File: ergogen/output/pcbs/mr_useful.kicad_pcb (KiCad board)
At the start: 2 copper layers, 57 x 95 mm, 36 parts

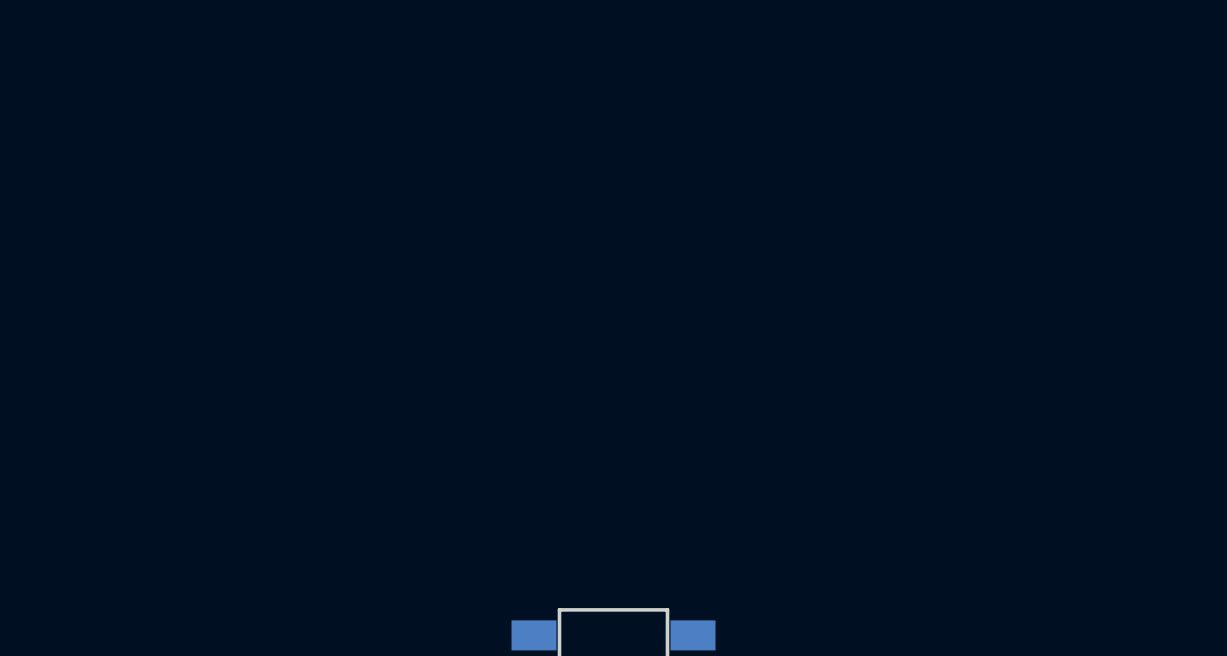
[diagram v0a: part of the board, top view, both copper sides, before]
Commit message: Add logo and reference
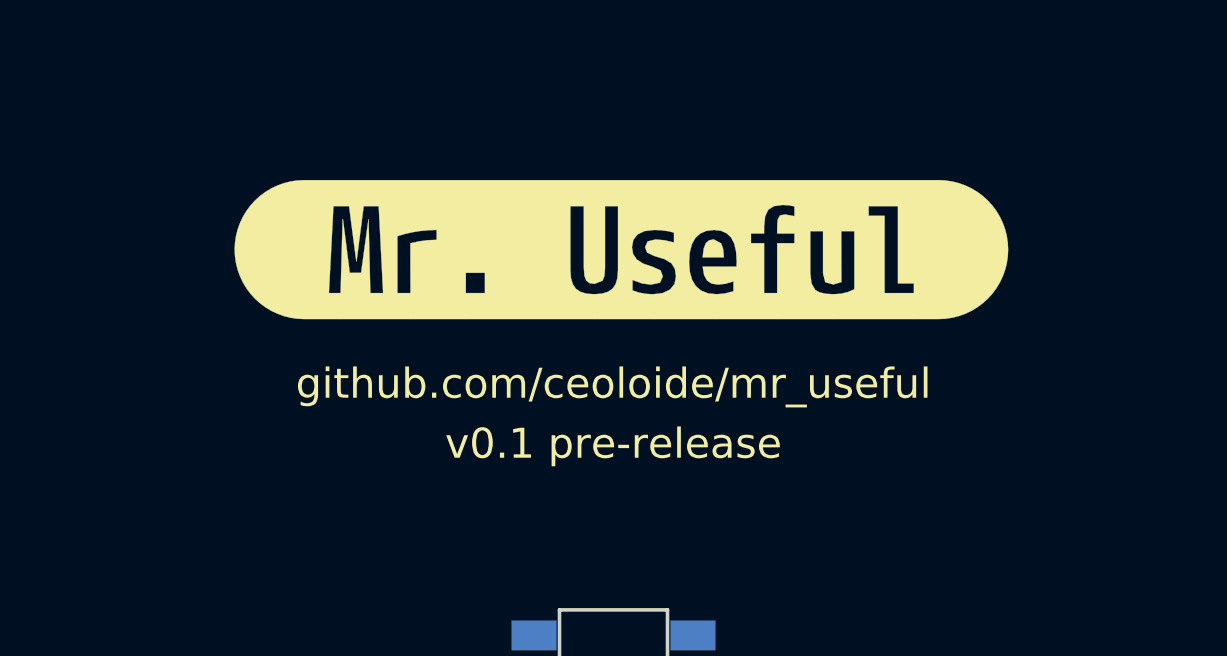
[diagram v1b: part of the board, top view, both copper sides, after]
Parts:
- added LOGO1: , logo_mr_useful, F.Cu at (79.0, 87.0)

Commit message: Update assets
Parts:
- LED1, LED10, LED2, LED3, LED4, LED5, LED6, LED7, LED8, LED9: footprint YS-SK6812MINI-E -> ceoloide:YS-SK6812MINI-E (per-key)
- LED11, LED12, LED13, LED14, LED15: footprint YS-SK6812MINI-E -> ceoloide:YS-SK6812MINI-E (underglow)

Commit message: Update assets
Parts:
- turned LED11 to 180 degrees
- turned LED12 to 180 degrees
- turned LED13 to 180 degrees
- turned LED14 to 180 degrees
- turned LED15 to 180 degrees

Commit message: Add JLCPCB order number text
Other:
- board text added: "JLCJLCJLCJLC"
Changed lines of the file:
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@@
         (layer F.SilkS) (width  0.01))
     )
+      (gr_text "JLCJLCJLCJLC" (at 79 87 0) (layer B.SilkS)
+        (effects (font (size 1 1) (thickness 0.15)) (justify mirror))
+      )
             (gr_line (start 51.5 134.5) (end 106.5 134.5) (angle 90) (layer Edge.Cuts) (width 0.15))
 (gr_line (start 107.5 133.5) (end 107.5 40.5) (angle 90) (layer Edge.Cuts) (width 0.15))

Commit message: Update assets
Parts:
- D1, D10, D2, D3, D4, D5, D6, D7, D8, D9: footprint ComboDiode -> ceoloide:diode_tht_sod123
- LED1, LED10, LED2, LED3, LED4, LED5, LED6, LED7, LED8, LED9: footprint ceoloide:YS-SK6812MINI-E (per-key) -> ceoloide:led_SK6812mini-e (per-keysingle-side)
- LED11, LED12, LED13, LED14, LED15: footprint ceoloide:YS-SK6812MINI-E (underglow) -> ceoloide:led_SK6812mini-e (underglowsingle-side)
